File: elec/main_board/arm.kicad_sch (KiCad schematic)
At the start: 30 parts, among them J13 B6B-ZR, J14 PinHeader, J15 PinHeader, J16 Fan motor, Q13 DMT6008LFG, SW6 TS-1088-AR02016, U17 FT231XQ-R, U19 INA219AIDCN, U20 ATmega328P-AU, X1 CSTCE16M0V53-R0

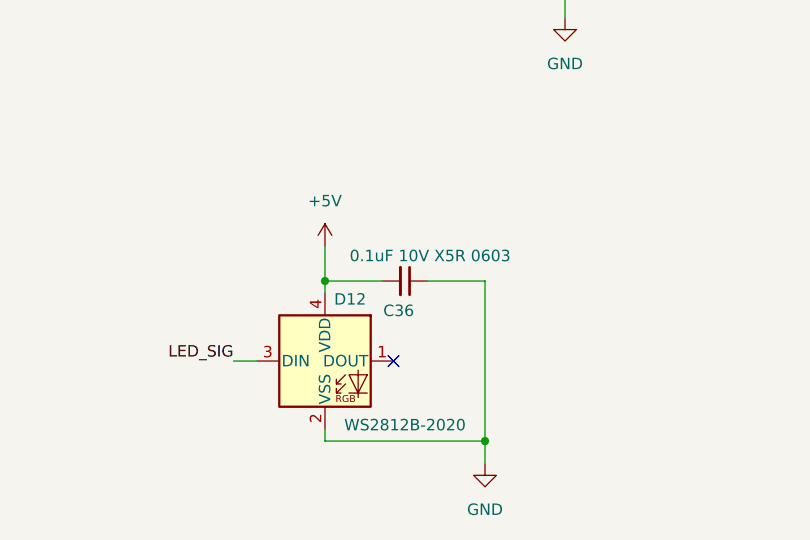
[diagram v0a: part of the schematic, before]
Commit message: 配線作業中
Signed-off-by: Kazuki Iida <elkel53930@gmail.com>
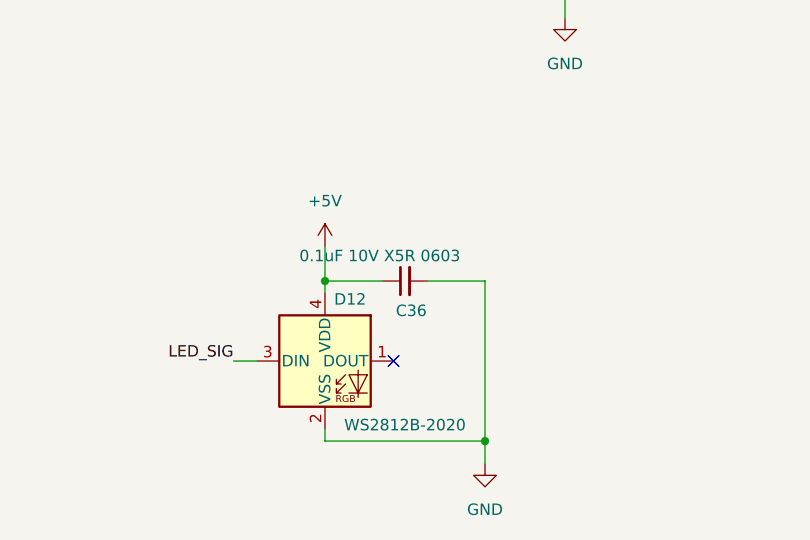
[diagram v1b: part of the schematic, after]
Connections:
- net +5V: now also C36.1; no longer C36.2
- net GND: now also C36.2; no longer C36.1
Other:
- moved on the sheet: C36
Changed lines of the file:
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@@
 	(symbol
 		(lib_id "Device:C_Small")
-		(at 82.55 200.66 270)
+		(at 82.55 200.66 90)
+		(mirror x)
 		(unit 1)
 		(exclude_from_sim no)
@@
 		(dnp no)
 		(property "Reference" "C36"
-			(at 83.566 203.962 90)
+			(at 81.534 203.962 90)
 			(effects
 				(font
@@
 		)
 		(property "Value" "GRM033R61A104KE15D"
-			(at 90.17 196.85 90)
+			(at 74.93 196.85 90)
 			(effects
 				(font
@@
 		)
 		(property "Description" "0.1uF 10V X5R 0603"
-			(at 85.344 197.866 90)
+			(at 79.756 197.866 90)
 			(effects
 				(font

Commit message: アートワーク完了
Signed-off-by: Kazuki Iida <elkel53930@gmail.com>
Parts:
- removed C48: RVT1A101M0505, Capacitor_SMD:CP_Elec_5x5.4, symbol Device:C_Polarized_Small
- removed J15: PinHeader, Connector_PinHeader_2.54mm:PinHeader_1x03_P2.54mm_Vertical, symbol Connector_Generic:Conn_01x03
- added C18, C49: CL32A107MPVNNNE, Capacitor_SMD:C_1210_3225Metric, symbol Device:C_Small
- added J7: B4B-ZR, Connector_JST:JST_ZH_B4B-ZR_1x04_P1.50mm_Vertical, symbol Connector_Generic:Conn_01x04
- added Q15: IRLML6344, Package_TO_SOT_SMD:SOT-23, symbol Transistor_FET:IRLML2060
- added R34, R36: 0603WAF1001T5E, Resistor_SMD:R_0603_1608Metric, symbol Device:R
- added R35: RC0201FR-0710KL, Resistor_SMD:R_0201_0603Metric, symbol Device:R
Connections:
- net +5V: now also C18.2, J7.1 (Pin_1), J7.3 (Pin_3)
- net +BATT: now also C49.2
- net GND: now also C18.1, C49.1, Q15.2 (S), R35.1, R36.2
- net BD_AD: now reaches U20.23 (PC0)
- net BD_AD: now also J7.4 (Pin_4), R36.1
- net SERVO_SIG2 renamed BD_EN
- net BD_EN: now also Q15.1 (G), R35.2
- new net: Q15.3 (D), R34.2
- new net: J7.2 (Pin_2), R34.1
- no-connect marks 20 -> 19
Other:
- note added: "A0"
